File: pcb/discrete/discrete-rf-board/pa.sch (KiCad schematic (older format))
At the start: 30 parts, among them J11 UFL, J12 UFL, J13 UFL, Q10 BFU520R

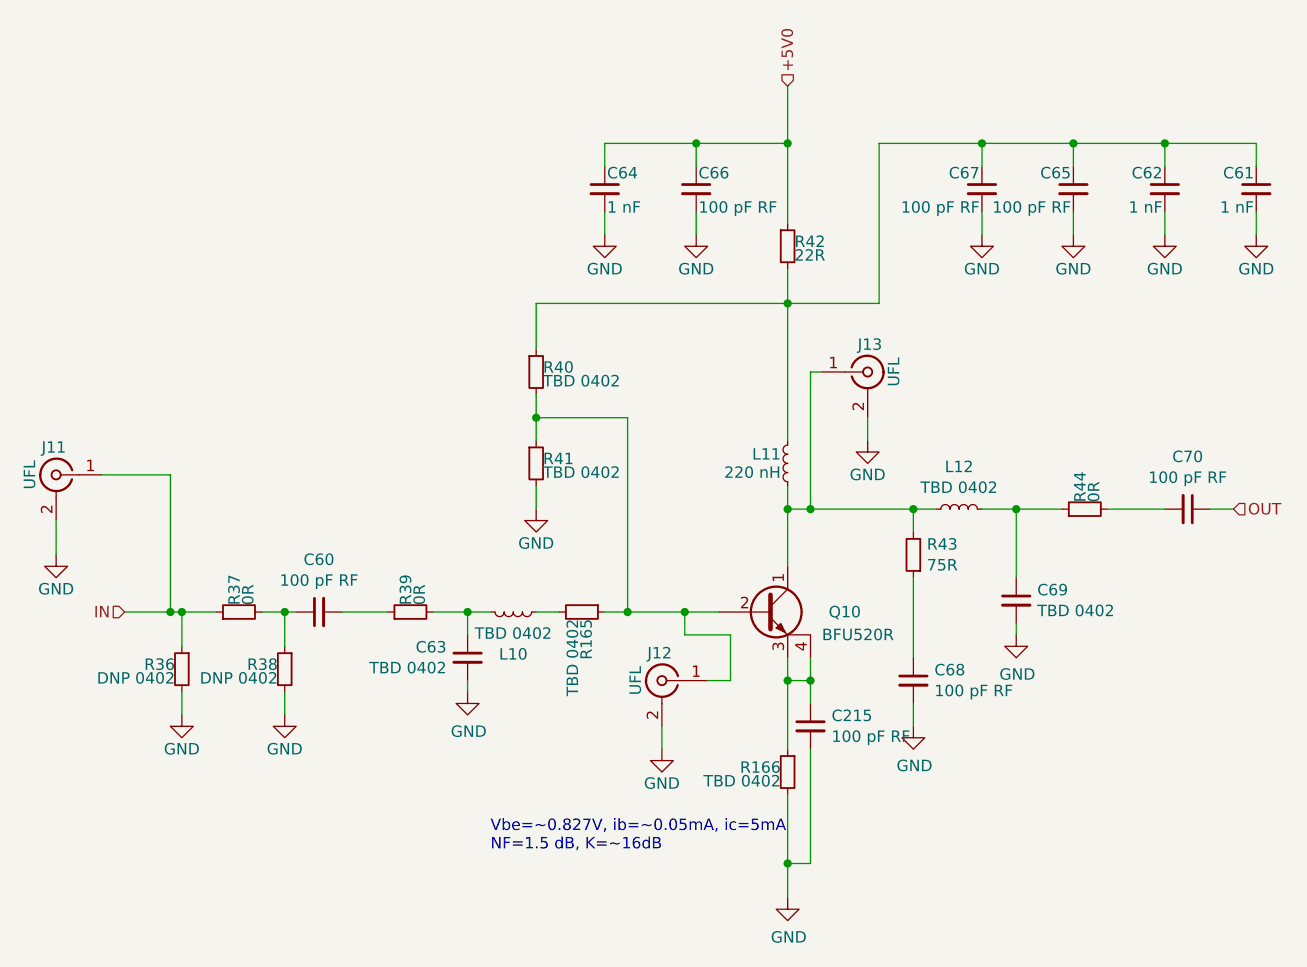
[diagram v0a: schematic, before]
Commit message: Reannotate everything; I'm trying to cut down the number of components
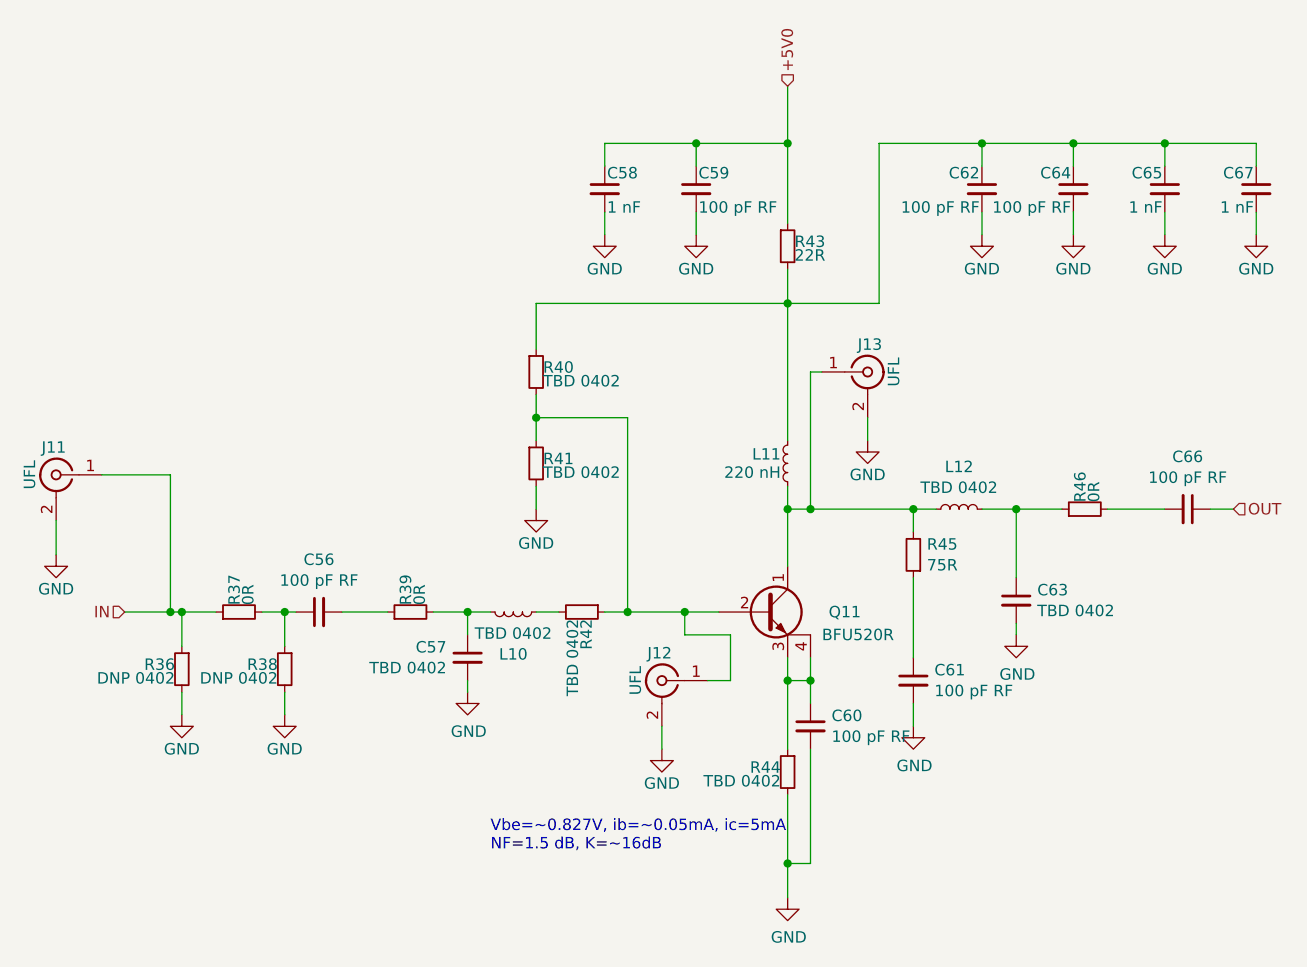
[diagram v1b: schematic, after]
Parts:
- renumbered C60 to C56, C63 to C57, C64 to C58, C66 to C59, C215 to C60, C68 to C61, C67 to C62, C69 to C63, C65 to C64, C62 to C65, C70 to C66, C61 to C67, Q10 to Q11, R165 to R42, R42 to R43, R166 to R44, R43 to R45, R44 to R46

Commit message: Footprint a lot of stuff; save before autofill
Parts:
- L11: footprint (none) -> Capacitor_SMD:C_0402_1005Metric; Mouser (none) -> 963-HK1005R22J-T
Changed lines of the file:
@@
 F 0 "L11" H 5680 3640 50  0000 L CNN
 F 1 "220 nH" H 5680 3560 50  0000 L CNN
-F 2 "" H 5650 3600 50  0001 C CNN
+F 2 "Capacitor_SMD:C_0402_1005Metric" H 5650 3600 50  0001 C CNN
 F 3 "~" H 5650 3600 50  0001 C CNN
+F 4 "963-HK1005R22J-T" H 5650 3600 50  0001 C CNN "Mouser"
 	1    5650 3600
 	-1   0    0    -1

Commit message: Autofill
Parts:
- C58, C65, C67: footprint (none) -> Capacitor_SMD:C_0402_1005Metric; Mouser (none) -> 80-C0402C102K5R7411
- R43: footprint (none) -> Resistor_SMD:R_0402_1005Metric; Mouser (none) -> 71-CRCW040222R0JNEDC
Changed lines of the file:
@@
 F 0 "C65" H 7310 2470 50  0000 L CNN
 F 1 "1 nF" H 7310 2320 50  0000 L CNN
-F 2 "" H 7300 2400 50  0001 C CNN
+F 2 "Capacitor_SMD:C_0402_1005Metric" H 7300 2400 50  0001 C CNN
 F 3 "~" H 7300 2400 50  0001 C CNN
+F 4 "80-C0402C102K5R7411" H 7300 2400 50  0001 C CNN "Mouser"
 	1    7300 2400
 	-1   0    0    -1
@@
 F 0 "C58" H 4860 2470 50  0000 L CNN
 F 1 "1 nF" H 4860 2320 50  0000 L CNN
-F 2 "" H 4850 2400 50  0001 C CNN
+F 2 "Capacitor_SMD:C_0402_1005Metric" H 4850 2400 50  0001 C CNN
 F 3 "~" H 4850 2400 50  0001 C CNN
+F 4 "80-C0402C102K5R7411" H 4850 2400 50  0001 C CNN "Mouser"
 	1    4850 2400
 	1    0    0    -1
@@
 F 0 "R43" H 5680 2670 50  0000 L CNN
 F 1 "22R" H 5680 2610 50  0000 L CNN
-F 2 "" H 5650 2650 50  0001 C CNN
+F 2 "Resistor_SMD:R_0402_1005Metric" H 5650 2650 50  0001 C CNN
 F 3 "~" H 5650 2650 50  0001 C CNN
+F 4 "71-CRCW040222R0JNEDC" H 5650 2650 50  0001 C CNN "Mouser"
 	1    5650 2650
 	1    0    0    -1
@@
 F 0 "C67" H 7710 2470 50  0000 L CNN
 F 1 "1 nF" H 7710 2320 50  0000 L CNN
-F 2 "" H 7700 2400 50  0001 C CNN
+F 2 "Capacitor_SMD:C_0402_1005Metric" H 7700 2400 50  0001 C CNN
 F 3 "~" H 7700 2400 50  0001 C CNN
+F 4 "80-C0402C102K5R7411" H 7700 2400 50  0001 C CNN "Mouser"
 	1    7700 2400
 	-1   0    0    -1

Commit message: Add in a couple more components, save before autofill
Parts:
- L12: footprint (none) -> Capacitor_SMD:C_0402_1005Metric; Mouser (none) -> NoPart
- R36: footprint (none) -> Resistor_SMD:R_0402_1005Metric; Mouser (none) -> NoPart
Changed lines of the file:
@@
 F 0 "L12" V 6585 3800 50  0000 C CNN
 F 1 "TBD 0402" V 6494 3800 50  0000 C CNN
-F 2 "" H 6400 3800 50  0001 C CNN
+F 2 "Capacitor_SMD:C_0402_1005Metric" H 6400 3800 50  0001 C CNN
 F 3 "~" H 6400 3800 50  0001 C CNN
+F 4 "NoPart" V 6400 3800 50  0001 C CNN "Mouser"
 	1    6400 3800
 	0    -1   -1   0
@@
 F 0 "R36" H 3030 4520 50  0000 L CNN
 F 1 "DNP 0402" H 3030 4460 50  0000 L CNN
-F 2 "" H 3000 4500 50  0001 C CNN
+F 2 "Resistor_SMD:R_0402_1005Metric" H 3000 4500 50  0001 C CNN
 F 3 "~" H 3000 4500 50  0001 C CNN
+F 4 "NoPart" H 3000 4500 50  0001 C CNN "Mouser"
 	1    3000 4500
 	-1   0    0    -1

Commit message: Autofill
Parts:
- L10: footprint (none) -> Capacitor_SMD:C_0402_1005Metric; Mouser (none) -> NoPart
- R38: footprint (none) -> Resistor_SMD:R_0402_1005Metric; Mouser (none) -> NoPart
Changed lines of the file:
@@
 F 0 "L10" V 4635 4250 50  0000 C CNN
 F 1 "TBD 0402" V 4544 4250 50  0000 C CNN
-F 2 "" H 4450 4250 50  0001 C CNN
+F 2 "Capacitor_SMD:C_0402_1005Metric" H 4450 4250 50  0001 C CNN
 F 3 "~" H 4450 4250 50  0001 C CNN
+F 4 "NoPart" H 4450 4250 50  0001 C CNN "Mouser"
 	1    4450 4250
 	0    -1   1    0
@@
 F 0 "R38" H 3480 4520 50  0000 L CNN
 F 1 "DNP 0402" H 3480 4460 50  0000 L CNN
-F 2 "" H 3450 4500 50  0001 C CNN
+F 2 "Resistor_SMD:R_0402_1005Metric" H 3450 4500 50  0001 C CNN
 F 3 "~" H 3450 4500 50  0001 C CNN
+F 4 "NoPart" H 3450 4500 50  0001 C CNN "Mouser"
 	1    3450 4500
 	-1   0    0    -1

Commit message: Footprint more stuff
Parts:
- R45: footprint (none) -> Resistor_SMD:R_0402_1005Metric; Mouser (none) -> 71-CRCW040275R0FKEDC
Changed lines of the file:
@@
 F 0 "R45" H 6141 3954 50  0000 R CNN
 F 1 "75R" H 6141 4045 50  0000 R CNN
-F 2 "" H 6200 4000 50  0001 C CNN
+F 2 "Resistor_SMD:R_0402_1005Metric" H 6200 4000 50  0001 C CNN
 F 3 "~" H 6200 4000 50  0001 C CNN
+F 4 "71-CRCW040275R0FKEDC" H 6200 4000 50  0001 C CNN "Mouser"
 	1    6200 4000
 	-1   0    0    1
